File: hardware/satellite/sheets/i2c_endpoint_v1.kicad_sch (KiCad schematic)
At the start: 20 parts, among them J1 RJHSE5380_QwiicBusCompatible, J7 Conn_01x04, U1 PCA9615DPZ, U4 USBLC6-4SC6

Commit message: Add qwiic connection for i2c expansion. Re-render the main assets
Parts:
- added J8: Qwiic, Connector_JST:JST_SH_BM04B-SRSS-TB_1x04-1MP_P1.00mm_Vertical, symbol project:Conn_01x04_StemmaQT
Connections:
- net GND: now also J8.1 (GND)
- net SAT_3V3: now also J8.2 (3v3)
- net SCL_LOCAL: now also J8.4 (SCL)
- net SDA_LOCAL: now also J8.3 (SDA)

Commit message: Improve Hub PCB layout, power loops, and sensing; add design review TODOs
- Hub PCB:
  - BQ25798 SW1/SW2 nodes: upgrade to 0.3mm neck with 3 parallel vias at IC and 2 at L1, plus B.Cu polygon pours
  - High-frequency loops: widen PMID and SYS connections with solid polygon pours to decoupling caps
  - Bootstrap caps: retain C317/C318 on F.Cu to preserve single-sided SMT assembly per TI 8.4.1 guidelines
  - Battery paths: cover U8 pins 22/23 with 0.8mm polygon pour and widen VBAT_RAW / VBAT_PROTECTED traces
  - Fuel gauge shunt: route FG_SRN and BATT_RTN as a 2.78mm matched parallel Kelvin pair from inner pad edges
  - ESP32-C5: rewire boot button SW2 to GPIO28; expose GPIO0 on header J7 pin 3
  - Flashing test points: add TP16-TP19 on B.Cu for single-sided bed-of-nails flashing
  - Layer balance: add full-board GND fill zone on In2.Cu and In3.Cu to balance copper density
- Add TODO tracking checklists for Satellite and Hub PCB reviews
- Add Hub pinout generator tool and update pinout documentation
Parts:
- JP11, JP14, JP15: now left out of the parts list
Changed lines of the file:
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@@
 		(body_style 1)
 		(exclude_from_sim no)
-		(in_bom yes)
+		(in_bom no)
 		(on_board yes)
-		(in_pos_files yes)
+		(in_pos_files no)
 		(dnp no)
 		(property "Reference" "JP14"
-			(at 95.25 191.77 0)
+			(at 97.79 179.07 0)
 			(show_name no)
 			(do_not_autoplace no)
@@
 		(body_style 1)
 		(exclude_from_sim no)
-		(in_bom yes)
+		(in_bom no)
 		(on_board yes)
-		(in_pos_files yes)
+		(in_pos_files no)
 		(dnp no)
 		(property "Reference" "JP15"
@@
 		(body_style 1)
 		(exclude_from_sim no)
-		(in_bom yes)
+		(in_bom no)
 		(on_board yes)
-		(in_pos_files yes)
+		(in_pos_files no)
 		(dnp no)
 		(property "Reference" "JP11"

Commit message: feat(hardware): complete satellite pcb routing and layout review fixes
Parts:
- added TP4, TP5: TestPoint_2Pole, project:TestPoint_2Pole_Pad_D1.0mm, symbol Connector:TestPoint_2Pole
- J7: Usage Auxiliary 2.54mm pin header exposing VCC_2 (Pin 1) and mult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 -> Auxiliary 1x4 2.54mm header: Pin 1: VCC_2, Pin 2: GND_2, Pi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
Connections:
- net DSCL_N: now also TP4.1
- net DSCL_P: now also TP4.2
- net DSDA_N: now also TP5.1
- net DSDA_P: now also TP5.2

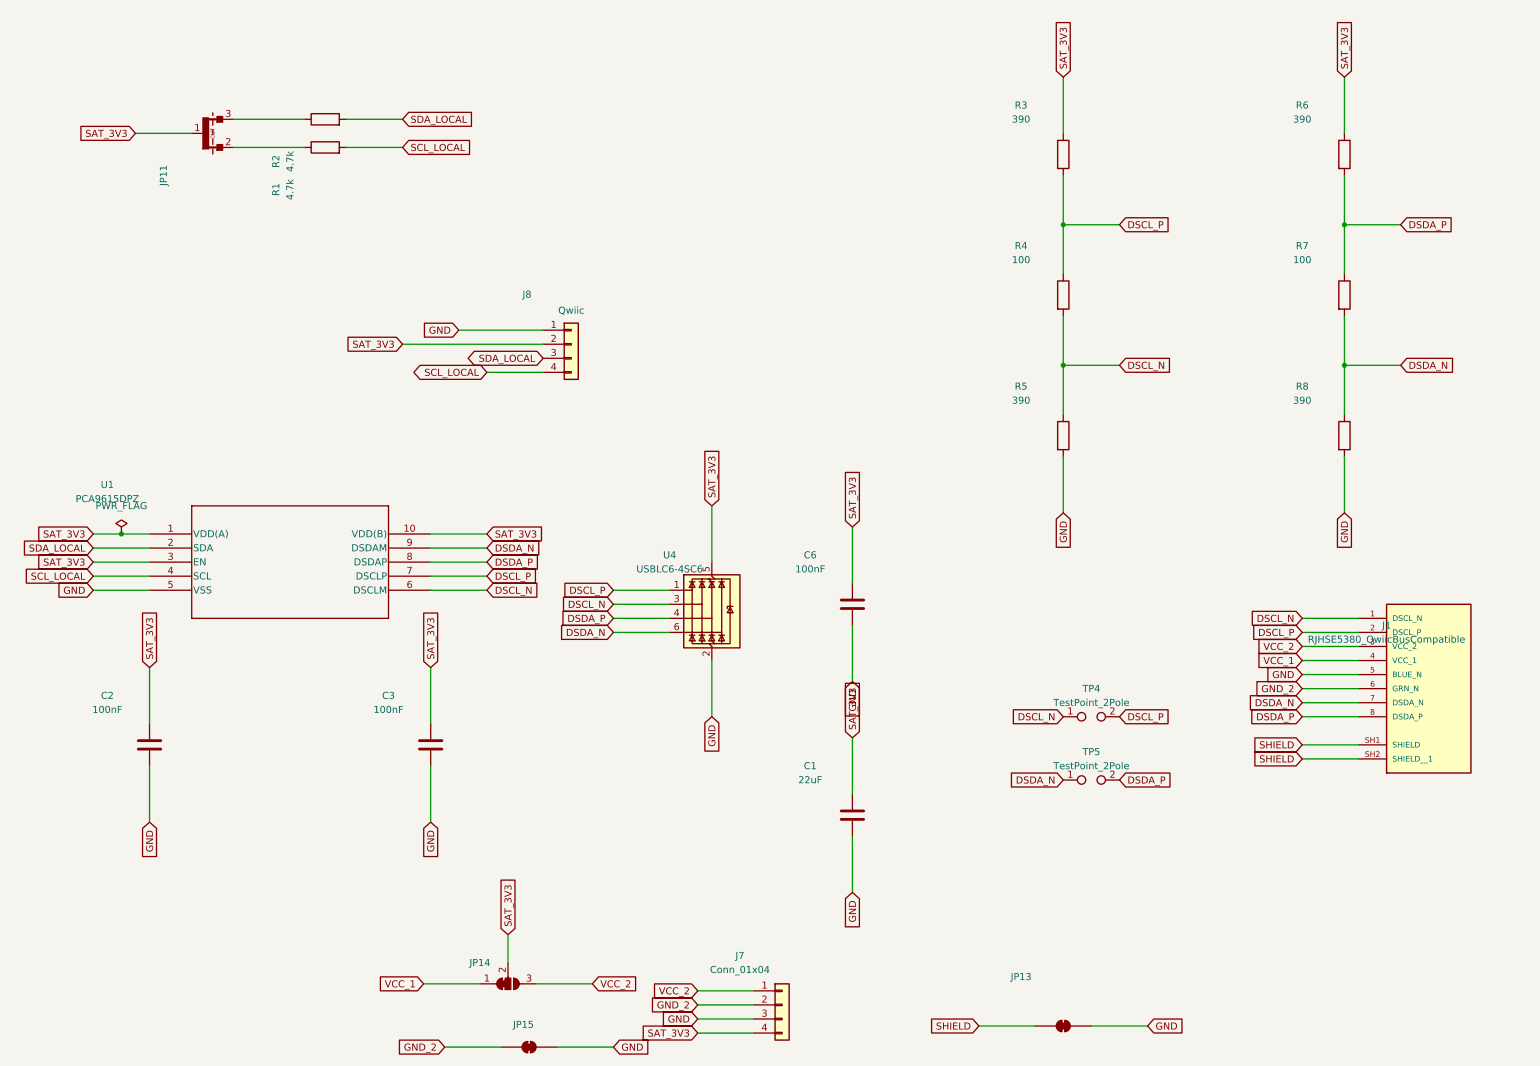
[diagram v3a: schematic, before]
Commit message: feat(satellite): redesign power entry architecture, solder jumpers, and address footprints
- Decouple raw cable power (Pair 1: RJ45_VCC_1/GND_1, Pair 3: RJ45_VCC_2/GND_2) onto 4P header J7
- Add 2P header J9 for local satellite power (SAT_3V3, GND) to support external regulation
- Add normally-closed cuttable jumpers JP18 (VCC_1 <-> SAT_3V3) and JP17 (GND_1 <-> GND)
- Tie PCA9615 VDDB, diff termination bias (R3/R5/R6/R8), and TVS U4 to RJ45_VCC_1/GND_1
- Place bulk cap C1 (22uF) across RJ45_VCC_1 and RJ45_GND_1 at cable entry
- Split inner planes: continuous RJ45_GND_1 reference on In2.Cu under B.Cu diff pairs; In1.Cu split (SAT GND, RJ45 GND, VCC2)
- Update 1-Wire address jumper footprint with +1/+2 bit-weighting notation and 0x18 default
- Remove deprecated pcb-pipeline generator scripts
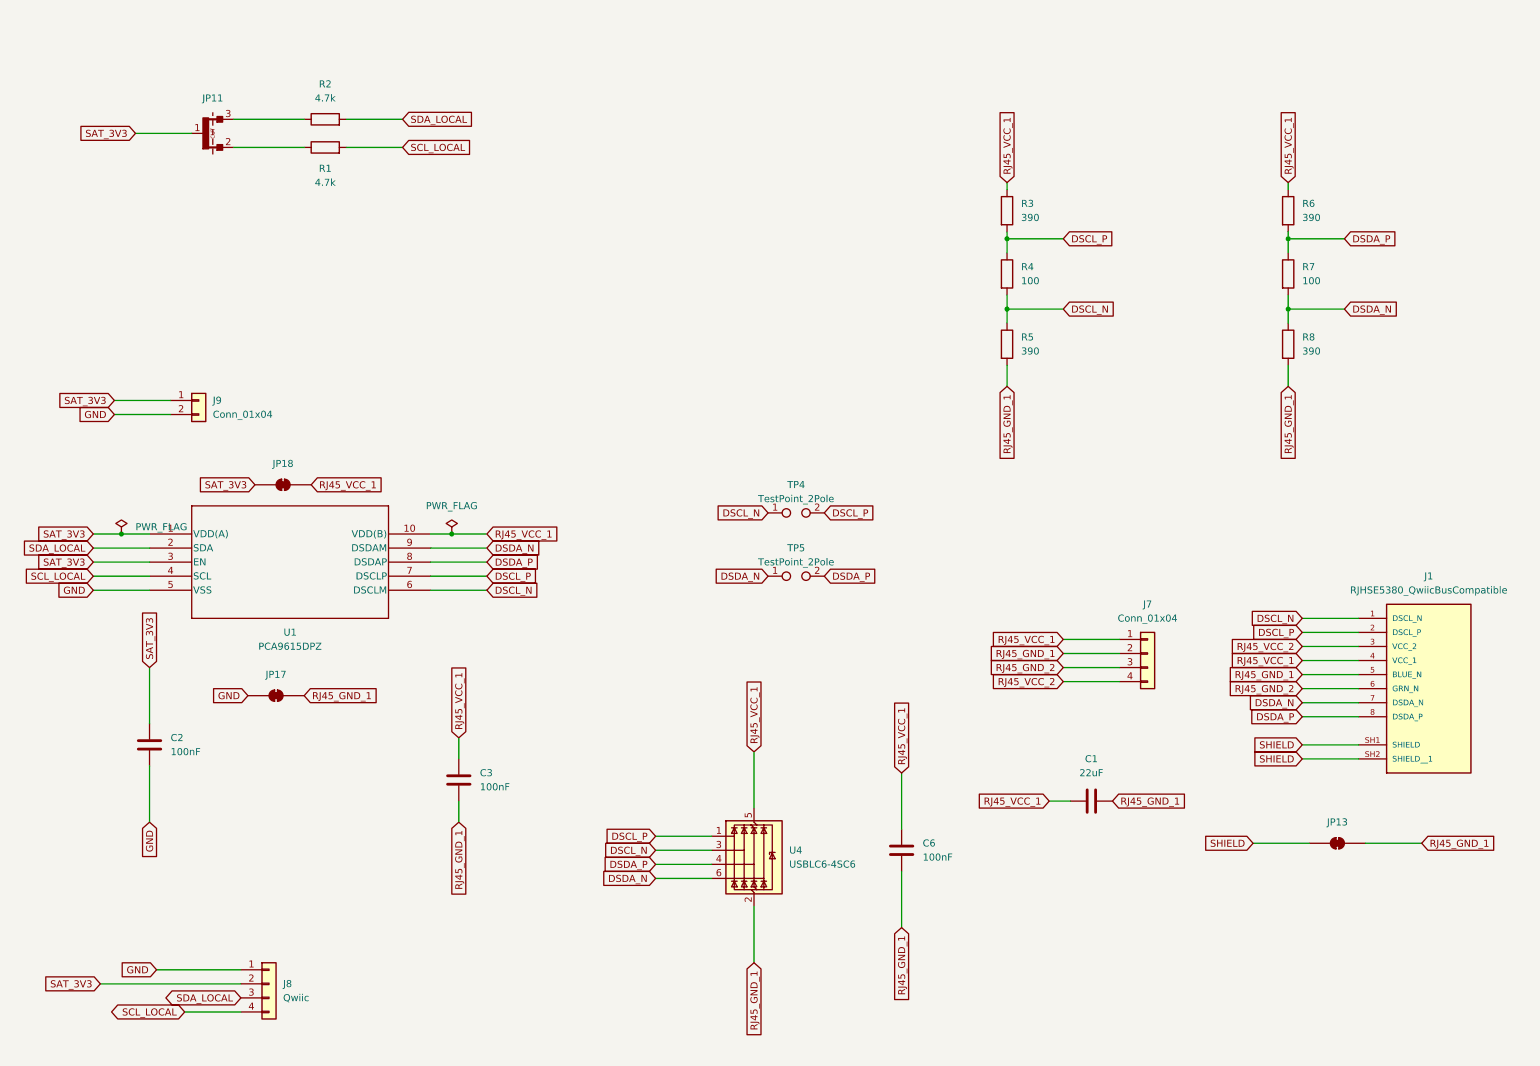
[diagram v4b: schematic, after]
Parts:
- removed JP14: SolderJumper_3_Bridged12, Jumper:SolderJumper-3_P1.3mm_Bridged12_RoundedPad1.0x1.5mm, symbol Jumper:SolderJumper_3_Bridged12
- removed JP15: SolderJumper_2_Bridged, Jumper:SolderJumper-2_P1.3mm_Bridged_RoundedPad1.0x1.5mm, symbol Jumper:SolderJumper_2_Bridged
- added J9: Conn_01x04, Connector_PinHeader_2.54mm:PinHeader_1x02_P2.54mm_Vertical, symbol Connector_Generic:Conn_01x02
- added JP17, JP18: SolderJumper_2_Bridged, Jumper:SolderJumper-2_P1.3mm_Bridged_RoundedPad1.0x1.5mm, symbol Jumper:SolderJumper_2_Bridged
- C1: footprint Capacitor_SMD:C_0805_2012Metric -> Capacitor_SMD:C_0805_2012Metric_Pad1.18x1.45mm_HandSolder
- C2, C3, C6: footprint Capacitor_SMD:C_0603_1608Metric -> Capacitor_SMD:C_0805_2012Metric_Pad1.18x1.45mm_HandSolder; LCSC Part C14663 -> C28233
- J7, JP13, TP4, TP5: now left out of the parts list
- J8: Supplier JLCPCB -> (none)
- R1, R2: footprint Resistor_SMD:R_0603_1608Metric -> Resistor_SMD:R_0805_2012Metric_Pad1.20x1.40mm_HandSolder; LCSC Part C23162 -> C17673
- R3, R5, R6, R8: footprint Resistor_SMD:R_0603_1608Metric -> Resistor_SMD:R_0805_2012Metric_Pad1.20x1.40mm_HandSolder; LCSC Part C23151 -> C17655
- R4, R7: footprint Resistor_SMD:R_0603_1608Metric -> Resistor_SMD:R_0805_2012Metric_Pad1.20x1.40mm_HandSolder; LCSC Part C22775 -> C17408
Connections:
- net GND: now also J9.2 (Pin_2), JP17.2 (B); no longer C1.2, C3.2, C6.2, J1.5 (BLUE_N), J7.3 (Pin_3), JP13.2 (B), R5.2, R8.2, U4.2 (GND)
- net SAT_3V3: now also J9.1 (Pin_1), JP18.2 (B); no longer C1.1, C3.1, C6.1, J7.4 (Pin_4), R3.1, R6.1, U1.10 (VDD(B)), U4.5 (VBUS)
- net GND_2 renamed RJ45_GND_1
- net RJ45_GND_1: now also C1.2, C3.2, C6.2, J1.5 (BLUE_N), JP13.2 (B), R5.2, R8.2, U4.2 (GND), JP17.1 (A); no longer J1.6 (GRN_N)
- net VCC_1 renamed RJ45_VCC_1
- net RJ45_VCC_1: now also C1.1, C3.1, C6.1, J7.1 (Pin_1), R3.1, R6.1, U1.10 (VDD(B)), U4.5 (VBUS), JP18.1 (A)
- net VCC_2 renamed RJ45_VCC_2
- net RJ45_VCC_2: now also J7.4 (Pin_4); no longer J7.1 (Pin_1)
- new net RJ45_GND_2: J1.6 (GRN_N), J7.3 (Pin_3)
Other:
- moved on the sheet: C1, C3, C6, J8, JP13, R3, R4, R5, R6, R7, R8, TP4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

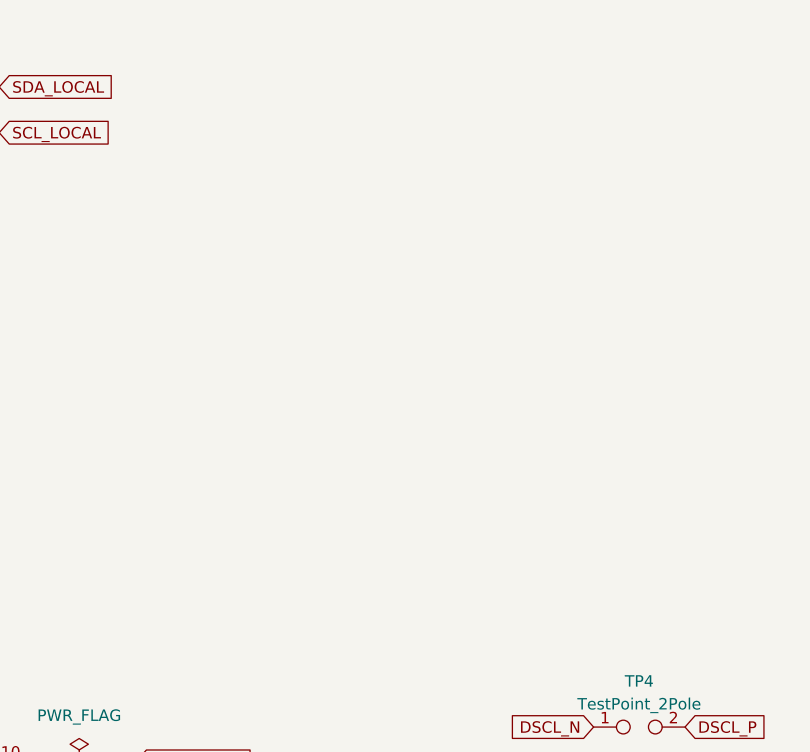
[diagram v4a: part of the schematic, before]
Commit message: feat(satellite): add power status LED1 and cuttable disconnect jumper JP19
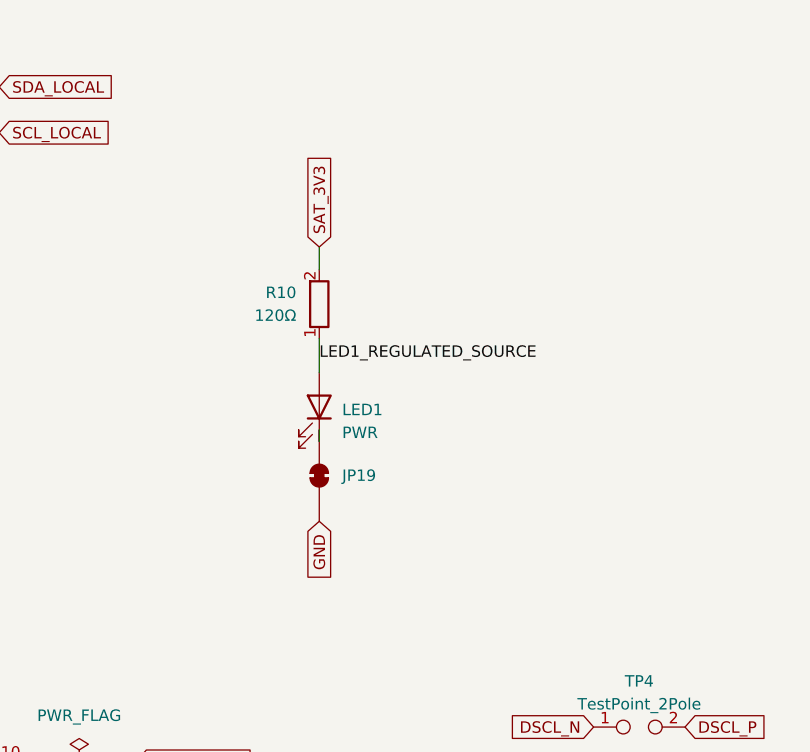
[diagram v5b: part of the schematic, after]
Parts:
- added JP19: SolderJumper_2_Bridged, Jumper:SolderJumper-2_P1.3mm_Bridged_RoundedPad1.0x1.5mm, symbol Jumper:SolderJumper_2_Bridged
- added LED1: PWR, LED_SMD:LED_0805_2012Metric_Pad1.15x1.40mm_HandSolder, symbol Device:LED
- added R10: 120Ω, Resistor_SMD:R_0805_2012Metric_Pad1.20x1.40mm_HandSolder, symbol Device:R
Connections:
- net GND: now also JP19.2 (B)
- net SAT_3V3: now also R10.2
- new net: JP19.1 (A), LED1.1 (K)
- new net LED1_REGULATED_SOURCE: LED1.2 (A), R10.1
